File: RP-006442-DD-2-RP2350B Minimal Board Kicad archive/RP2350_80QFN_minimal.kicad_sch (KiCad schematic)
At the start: 50 parts, among them J1 USB_C_Receptacle_USB2.0_16P, J2 Conn_02x26_Odd_Even, J3 Conn_02x26_Odd_Even, SW1 SW_Push, SW2 SW_Push, U1 RP2350_80QFN, U2 NCP1117-3.3_SOT223, U3 W25Q128JVS, U4 DNF, Y1 ABM8-272-T3

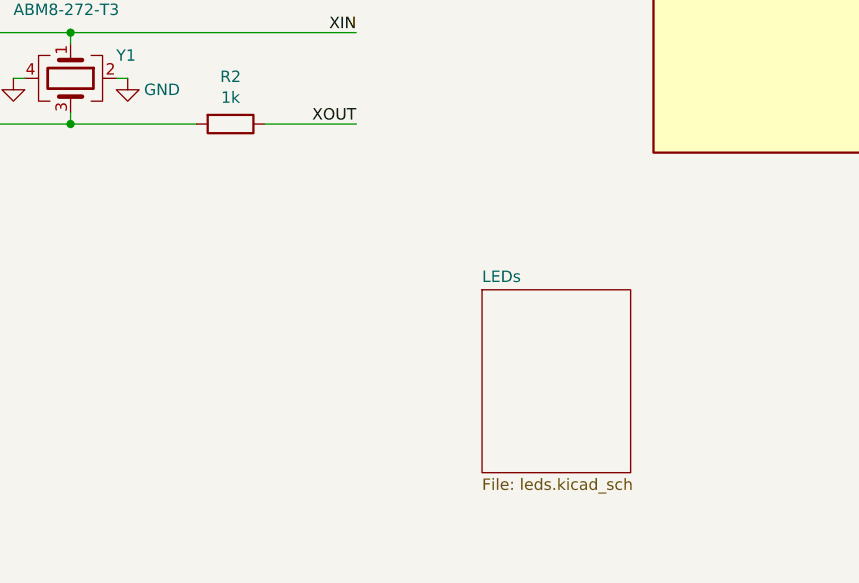
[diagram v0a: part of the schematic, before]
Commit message: LED Sheet , Two Buttons
Attempt at completing LED sheet with resistors and GPIO connections.
Also two buttons in the Button sheet.
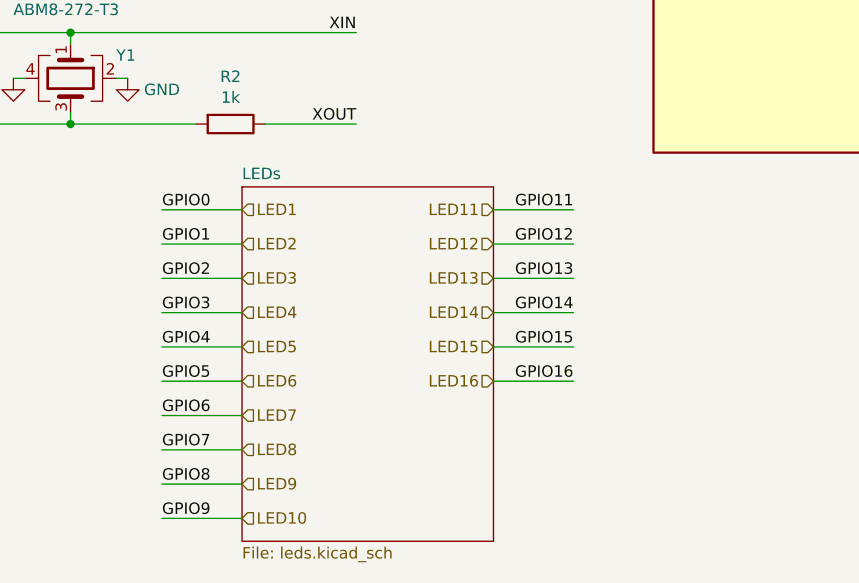
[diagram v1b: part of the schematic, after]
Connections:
- net GPIO0 renamed LED1
- net GPIO1 renamed LED2
- net GPIO11 renamed LED11
- net GPIO12 renamed LED12
- net GPIO13 renamed LED13
- net GPIO14 renamed LED14
- net GPIO15 renamed LED15
- net GPIO16 renamed LED16
- net GPIO2 renamed LED3
- net GPIO3 renamed LED4
- net GPIO4 renamed LED5
- net GPIO5 renamed LED6
- net GPIO6 renamed LED7
- net GPIO7 renamed LED8
- net GPIO8 renamed LED9
- net GPIO9 renamed LED10

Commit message: leds
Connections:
- net GPIO10 is gone; now on net LED9: J2.24 (Pin_24), U1.8 (GPIO10)
- net GPIO17 is gone; now on net LED16: J2.38 (Pin_38), U1.17 (GPIO17)
- net LED1: now also J2.8 (Pin_8), U1.79 (GPIO2); no longer J2.4 (Pin_4), R11.1, R9.1, U1.77 (GPIO0)
- net LED10: now also J2.26 (Pin_26), U1.9 (GPIO11); no longer J2.22 (Pin_22), U1.7 (GPIO9)
- net LED11: now also J2.28 (Pin_28), U1.11 (GPIO12); no longer J2.26 (Pin_26), U1.9 (GPIO11)
- net LED12: now also J2.30 (Pin_30), U1.12 (GPIO13); no longer J2.28 (Pin_28), U1.11 (GPIO12)
- net LED13: now also J2.32 (Pin_32), U1.13 (GPIO14); no longer J2.30 (Pin_30), U1.12 (GPIO13)
- net LED14: now also J2.34 (Pin_34), U1.14 (GPIO15); no longer J2.32 (Pin_32), U1.13 (GPIO14)
- net LED15: now also J2.36 (Pin_36), U1.16 (GPIO16); no longer J2.34 (Pin_34), U1.14 (GPIO15)
- net LED16: no longer J2.36 (Pin_36), U1.16 (GPIO16)
- net LED2: now also J2.10 (Pin_10), U1.80 (GPIO3); no longer J2.6 (Pin_6), U1.78 (GPIO1)
- net LED3: now also J2.12 (Pin_12), U1.1 (GPIO4); no longer J2.8 (Pin_8), U1.79 (GPIO2)
- net LED4: now also J2.14 (Pin_14), U1.2 (GPIO5); no longer J2.10 (Pin_10), U1.80 (GPIO3)
- net LED5: now also J2.16 (Pin_16), U1.3 (GPIO6); no longer J2.12 (Pin_12), U1.1 (GPIO4)
- net LED6: now also J2.18 (Pin_18), U1.4 (GPIO7); no longer J2.14 (Pin_14), U1.2 (GPIO5)
- net LED7: now also J2.20 (Pin_20), U1.6 (GPIO8); no longer J2.16 (Pin_16), U1.3 (GPIO6)
- net LED8: now also J2.22 (Pin_22), U1.7 (GPIO9); no longer J2.18 (Pin_18), U1.4 (GPIO7)
- net LED9: no longer J2.20 (Pin_20), U1.6 (GPIO8)
- new net GPIO0: J2.4 (Pin_4), R11.1, R9.1, U1.77 (GPIO0)
- new net GPIO1: J2.6 (Pin_6), U1.78 (GPIO1)
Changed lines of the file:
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@@
 		)
 	)
-	(label "GPIO11"
+	(label "GPIO12"
 		(at 160.02 245.11 180)
 		(effects
@@
 		)
 	)
-	(label "GPIO7"
+	(label "GPIO9"
 		(at 114.3 271.78 0)
 		(effects
@@
 		)
 	)
-	(label "GPIO2"
+	(label "GPIO4"
 		(at 114.3 252.73 0)
 		(effects
@@
 		)
 	)
-	(label "GPIO12"
+	(label "GPIO13"
 		(at 160.02 248.92 180)
 		(effects
@@
 		)
 	)
-	(label "GPIO15"
+	(label "GPIO16"
 		(at 160.02 260.35 180)
 		(effects
@@
 		)
 	)
-	(label "GPIO0"
+	(label "GPIO2"
 		(at 114.3 245.11 0)
 		(effects
@@
 		)
 	)
-	(label "GPIO5"
+	(label "GPIO7"
 		(at 114.3 264.16 0)
 		(effects
@@
 		)
 	)
-	(label "GPIO3"
+	(label "GPIO5"
 		(at 114.3 256.54 0)
 		(effects
@@
 		)
 	)
-	(label "GPIO14"
+	(label "GPIO15"
 		(at 160.02 256.54 180)
 		(effects
@@
 		)
 	)
-	(label "GPIO9"
+	(label "GPIO11"
 		(at 114.3 279.4 0)
 		(effects
@@
 		)
 	)
-	(label "GPIO13"
+	(label "GPIO14"
 		(at 160.02 252.73 180)
 		(effects
@@
 		)
 	)
-	(label "GPIO1"
+	(label "GPIO3"
 		(at 114.3 248.92 0)
 		(effects
@@
 		)
 	)
-	(label "GPIO6"
+	(label "GPIO8"
 		(at 114.3 267.97 0)
 		(effects
@@
 		)
 	)
-	(label "GPIO4"
+	(label "GPIO6"
 		(at 114.3 260.35 0)
 		(effects
@@
 		)
 	)
-	(label "GPIO16"
+	(label "GPIO17"
 		(at 160.02 264.16 180)
 		(effects
@@
 		)
 	)
-	(label "GPIO8"
+	(label "GPIO10"
 		(at 114.3 275.59 0)
 		(effects

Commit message: Update RP2350_80QFN_minimal.kicad_sch
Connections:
- net LED1 renamed GPIO2
- net LED10 renamed GPIO11
- net LED11 renamed GPIO12
- net LED12 renamed GPIO13
- net LED13 renamed GPIO14
- net LED14 renamed GPIO15
- net LED15 renamed GPIO16
- net LED16 renamed GPIO17
- net LED2 renamed GPIO3
- net LED3 renamed GPIO4
- net LED4 renamed GPIO5
- net LED5 renamed GPIO6
- net LED6 renamed GPIO7
- net LED7 renamed GPIO8
- net LED8 renamed GPIO9
- net LED9 renamed GPIO10
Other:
- sheet LEDs ports: added Master reset, Output enable, Serial data input, Shift register clock input, Storage register clock input, Vcc; removed none
- moved on the sheet: J2, J3

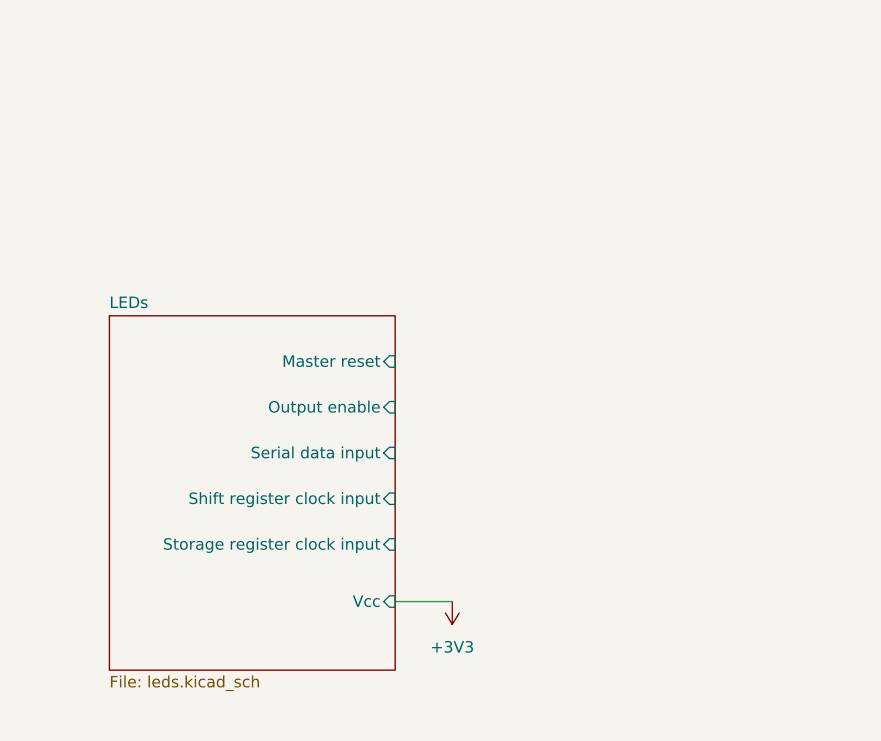
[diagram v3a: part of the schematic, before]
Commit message: Connected GPIOs to Shift Register pins
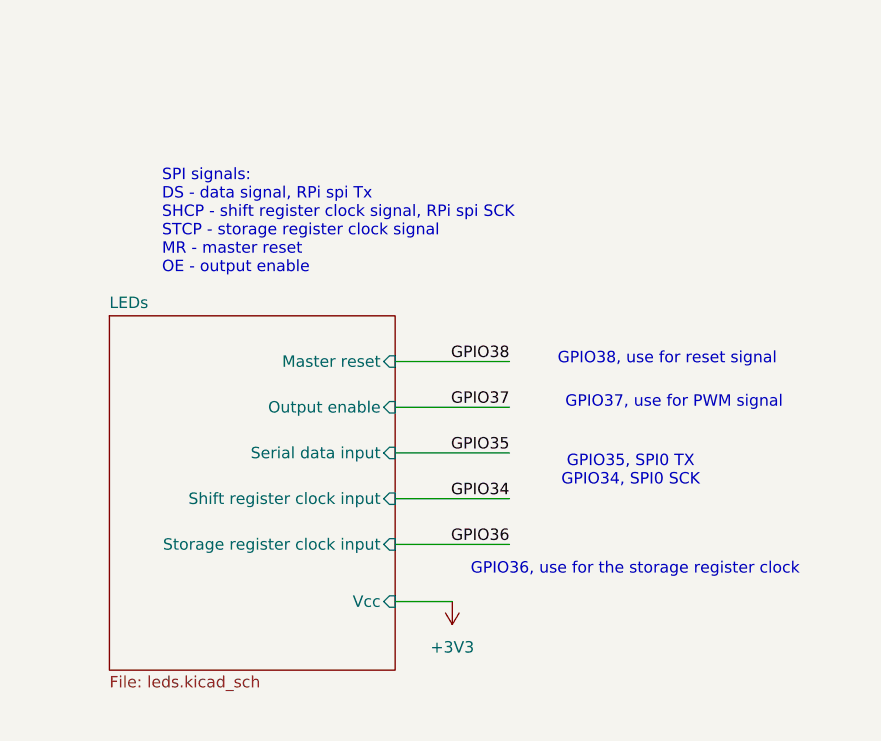
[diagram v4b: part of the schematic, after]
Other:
- note added: "GPIO35, SPI0 TX GPIO34, SPI0 SCK"
- note added: "GPIO36, use for the storage register clock"
- note added: "GPIO37, use for PWM signal"
- note added: "GPIO38, use for reset signal"
- note added: "SPI signals: DS - data signal, RPi spi Tx SHCP - shift register clock signal, RPi spi SCK STCP - storage register clock signal MR - master reset OE - output enable"
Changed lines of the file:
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@@
 		)
 	)
+	(text "GPIO36, use for the storage register clock"
+		(exclude_from_sim no)
+		(at 386.08 227.584 0)
+		(effects
+			(font
+				(size 1.27 1.27)
+			)
+		)
+	)
 	(text "12MHz Crystal"
 		(exclude_from_sim no)
@@
 		)
 	)
+	(text "GPIO35, SPI0 TX\nGPIO34, SPI0 SCK"
+		(exclude_from_sim no)
+		(at 385.572 216.662 0)
+		(effects
+			(font
+				(size 1.27 1.27)
+			)
+		)
+	)
 	(text "Primary Flash"
 		(exclude_from_sim no)
@@
 		)
 	)
+	(text "SPI signals:\nDS - data signal, RPi spi Tx\nSHCP - shift register clock signal, RPi spi SCK\nSTCP - storage register clock signal\nMR - master reset\nOE - output enable"
+		(exclude_from_sim no)
+		(at 333.502 188.976 0)
+		(effects
+			(font
+				(size 1.27 1.27)
+			)
+			(justify left)
+		)
+	)
+	(text "GPIO37, use for PWM signal"
+		(exclude_from_sim no)
+		(at 390.398 209.042 0)
+		(effects
+			(font
+				(size 1.27 1.27)
+			)
+		)
+	)
 	(text "Power"
 		(exclude_from_sim no)
@@
 		)
 	)
+	(text "GPIO38, use for reset signal\n"
+		(exclude_from_sim no)
+		(at 389.636 204.216 0)
+		(effects
+			(font
+				(size 1.27 1.27)
+			)
+		)
+	)
 	(junction
 		(at 119.38 115.57)
@@
 	(wire
 		(pts
+			(xy 372.11 224.79) (xy 359.41 224.79)
+		)
+		(stroke
+			(width 0)
+			(type default)
+		)
+	)
+	(wire
+		(pts
 			(xy 234.95 231.14) (xy 250.19 231.14)
 		)
@@
 	(wire
 		(pts
+			(xy 372.11 204.47) (xy 359.41 204.47)
+		)
+		(stroke
+			(width 0)
+			(type default)
+		)
+	)
+	(wire
+		(pts
 			(xy 322.58 90.17) (xy 322.58 92.71)
 		)
@@
 	(wire
 		(pts
+			(xy 372.11 219.71) (xy 359.41 219.71)
+		)
+		(stroke
+			(width 0)
+			(type default)
+		)
+	)
+	(wire
+		(pts
 			(xy 394.97 135.89) (xy 394.97 138.43)
 		)
@@
 	(wire
 		(pts
+			(xy 372.11 214.63) (xy 359.41 214.63)
+		)
+		(stroke
+			(width 0)
+			(type default)
+		)
+	)
+	(wire
+		(pts
 			(xy 323.85 105.41) (xy 322.58 105.41)
 		)
@@
 	(wire
 		(pts
+			(xy 372.11 209.55) (xy 359.41 209.55)
+		)
+		(stroke
+			(width 0)
+			(type default)
+		)
+	)
+	(wire
+		(pts
 			(xy 273.05 195.58) (xy 281.94 195.58)
 		)
@@
 		)
 	)
+	(label "GPIO36"
+		(at 372.11 224.79 180)
+		(effects
+			(font
+				(size 1.27 1.27)
+			)
+			(justify right bottom)
+		)
+	)
 	(label "QSPI_SD0"
 		(at 92.71 122.555 180)
@@
 		)
 	)
+	(label "GPIO38"
+		(at 372.11 204.47 180)
+		(effects
+			(font
+				(size 1.27 1.27)
+			)
+			(justify right bottom)
+		)
+	)
+	(label "GPIO35"
+		(at 372.11 214.63 180)
+		(effects
+			(font
+				(size 1.27 1.27)
+			)
+			(justify right bottom)
+		)
+	)
 	(label "GPIO47_ADC7"
 		(at 250.19 233.68 180)
@@
 		)
 	)
+	(label "GPIO37"
+		(at 372.11 209.55 180)
+		(effects
+			(font
+				(size 1.27 1.27)
+			)
+			(justify right bottom)
+		)
+	)
 	(label "SWD"
 		(at 273.05 198.12 0)
@@
 		(effects
 			(font
+				(size 1.27 1.27)
+			)
+			(justify right bottom)
+		)
+	)
+	(label "GPIO34"
+		(at 372.11 219.71 180)
+		(effects
+			(font

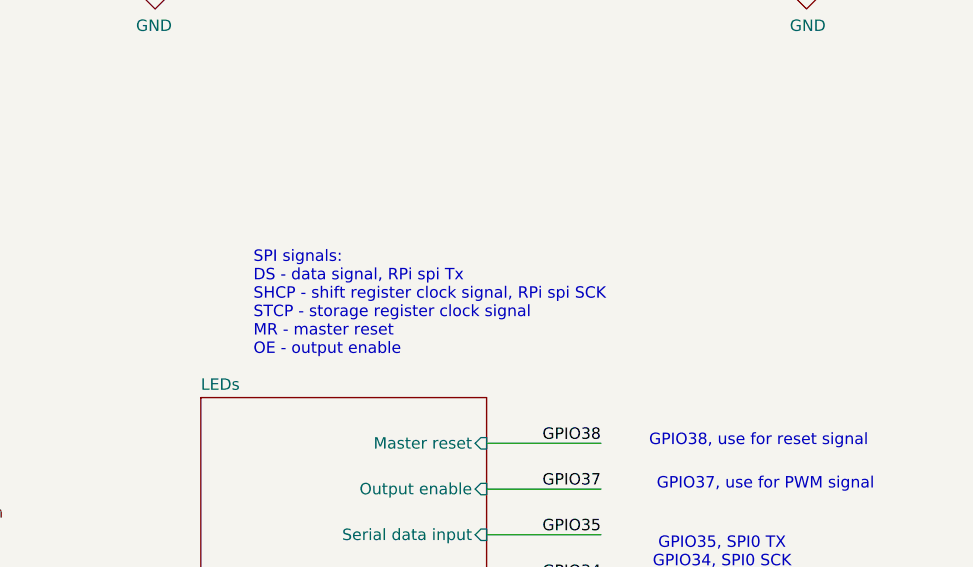
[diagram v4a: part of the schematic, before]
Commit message: Update RP2350_80QFN_minimal.kicad_sch
added some description text
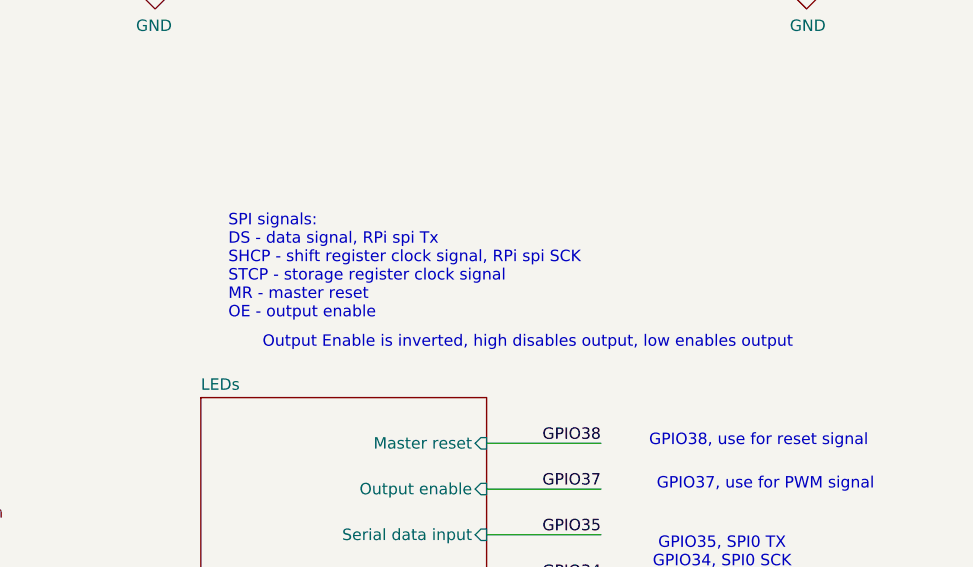
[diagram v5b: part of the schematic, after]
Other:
- note added: "Output Enable is inverted, high disables output, low enables output"
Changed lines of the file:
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@@
 	(text "SPI signals:\nDS - data signal, RPi spi Tx\nSHCP - shift register clock signal, RPi spi SCK\nSTCP - storage register clock signal\nMR - master reset\nOE - output enable"
 		(exclude_from_sim no)
-		(at 333.502 188.976 0)
+		(at 330.708 184.912 0)
 		(effects
 			(font
@@
 		)
 	)
+	(text "Output Enable is inverted, high disables output, low enables output"
+		(exclude_from_sim no)
+		(at 363.982 193.294 0)
+		(effects
+			(font
+				(size 1.27 1.27)
+			)
+		)
+	)

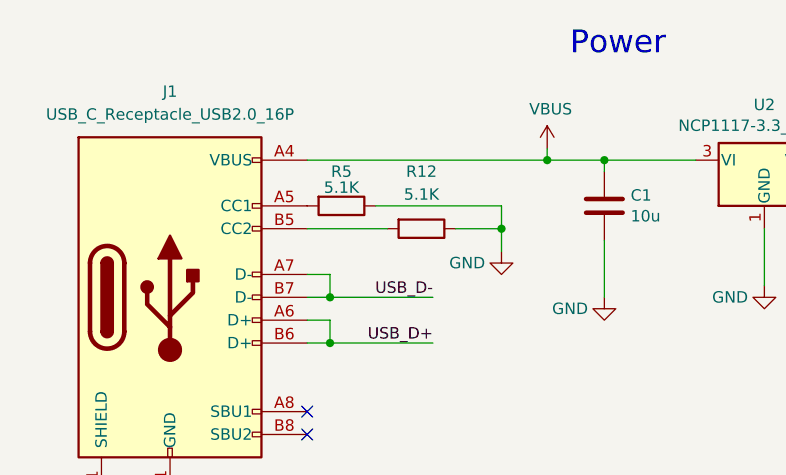
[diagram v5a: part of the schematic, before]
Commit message: Update to schematic and pcb
Changed ht16k33 package from 28SOP to 24SSOP

Placed pcb footprints
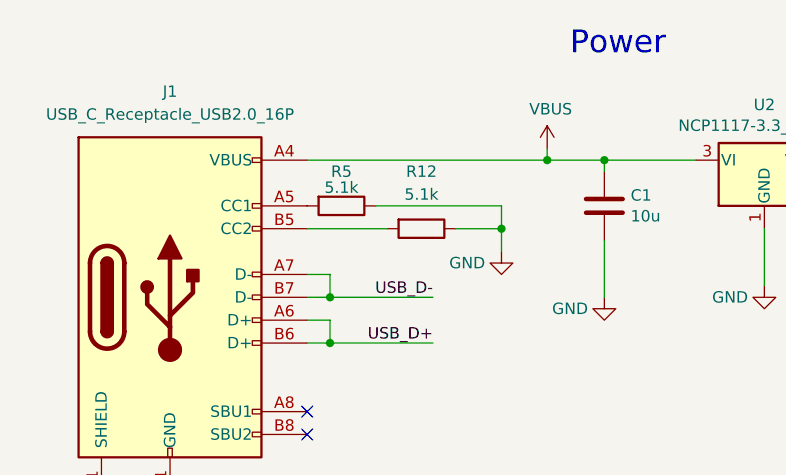
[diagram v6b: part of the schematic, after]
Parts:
- R12, R5: value 5.1K -> 5.1k
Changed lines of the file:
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@@
 			)
 		)
-		(property "Value" "5.1K"
+		(property "Value" "5.1k"
 			(at 48.26 42.418 90)
 			(effects
@@
 			)
 		)
-		(property "Value" "5.1K"
+		(property "Value" "5.1k"
 			(at 57.15 43.18 90)
 			(effects

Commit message: Update
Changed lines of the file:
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@@
 	(wire
 		(pts
+			(xy 269.24 229.87) (xy 274.32 229.87)
+		)
+		(stroke
+			(width 0)
+			(type default)
+		)
+	)
+	(wire
+		(pts
 			(xy 394.97 100.33) (xy 394.97 102.87)
 		)
@@
 	)
 	(symbol
+		(lib_id "power:VBUS")
+		(at 269.24 229.87 0)
+		(unit 1)
+		(exclude_from_sim no)
+		(in_bom yes)
+		(on_board yes)
+		(dnp no)
+		(property "Reference" "#PWR032"
+			(at 269.24 233.68 0)
+			(effects
+				(font
+					(size 1.27 1.27)
+				)
+				(hide yes)
+			)
+		)
+		(property "Value" "VBUS"
+			(at 269.621 225.4758 0)
+			(effects
+				(font
+					(size 1.27 1.27)
+				)
+			)
+		)
+		(property "Footprint" ""
+			(at 269.24 229.87 0)
+			(effects
+				(font
+					(size 1.27 1.27)
+				)
+				(hide yes)
+			)
+		)
+		(property "Datasheet" ""
+			(at 269.24 229.87 0)
+			(effects
+				(font
+					(size 1.27 1.27)
+				)
+				(hide yes)
+			)
+		)
+		(property "Description" ""
+			(at 269.24 229.87 0)
+			(effects
+				(font
+					(size 1.27 1.27)
+				)
+				(hide yes)
+			)
+		)
+		(pin "1"
+		)
+		(instances
+			(project "RP2350_80QFN_minimal"
+				(path "/94683f5c-9cd9-448e-be96-9792537b5cb8"
+					(reference "#PWR032")
+					(unit 1)
+				)
+			)
+		)
+	)
+	(symbol
 		(lib_id "power:GND")
 		(at 66.04 49.53 0)
@@
 		)
 		(pin "SCL" input
-			(at 274.32 231.14 180)
+			(at 274.32 240.03 180)
 			(effects
 				(font
@@
 		)
 		(pin "VDD" input
-			(at 274.32 240.03 180)
+			(at 274.32 229.87 180)
 			(effects
 				(font

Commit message: Update
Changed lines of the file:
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@@
 	(wire
 		(pts
-			(xy 269.24 229.87) (xy 274.32 229.87)
-		)
-		(stroke
-			(width 0)
-			(type default)
-		)
-	)
-	(wire
-		(pts
 			(xy 394.97 100.33) (xy 394.97 102.87)
 		)
@@
 	)
 	(symbol
-		(lib_id "power:VBUS")
-		(at 269.24 229.87 0)
-		(unit 1)
-		(exclude_from_sim no)
-		(in_bom yes)
-		(on_board yes)
-		(dnp no)
-		(property "Reference" "#PWR032"
-			(at 269.24 233.68 0)
-			(effects
-				(font
-					(size 1.27 1.27)
-				)
-				(hide yes)
-			)
-		)
-		(property "Value" "VBUS"
-			(at 269.621 225.4758 0)
-			(effects
-				(font
-					(size 1.27 1.27)
-				)
-			)
-		)
-		(property "Footprint" ""
-			(at 269.24 229.87 0)
-			(effects
-				(font
-					(size 1.27 1.27)
-				)
-				(hide yes)
-			)
-		)
-		(property "Datasheet" ""
-			(at 269.24 229.87 0)
-			(effects
-				(font
-					(size 1.27 1.27)
-				)
-				(hide yes)
-			)
-		)
-		(property "Description" ""
-			(at 269.24 229.87 0)
-			(effects
-				(font
-					(size 1.27 1.27)
-				)
-				(hide yes)
-			)
-		)
-		(pin "1"
-		)
-		(instances
-			(project "RP2350_80QFN_minimal"
-				(path "/94683f5c-9cd9-448e-be96-9792537b5cb8"
-					(reference "#PWR032")
-					(unit 1)
-				)
-			)
-		)
-	)
-	(symbol
 		(lib_id "power:GND")
 		(at 66.04 49.53 0)
@@
 		)
 		(pin "SCL" input
-			(at 274.32 240.03 180)
+			(at 274.32 231.14 180)
 			(effects
 				(font
@@
 		)
 		(pin "VDD" input
-			(at 274.32 229.87 180)
+			(at 274.32 240.03 180)
 			(effects
 				(font
